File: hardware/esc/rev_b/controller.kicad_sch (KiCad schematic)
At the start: 47 parts, among them J201 ESC_SWD, U201 RP2354B, U204 TPS3430WDRCR, U205 SN74LVC1G08DBVR, U206 TCAN3413DR, U207 MCP2518FD-H/QBB, Y201 12MHz ABM8-272-T3, Y202 40MHz ABM8G

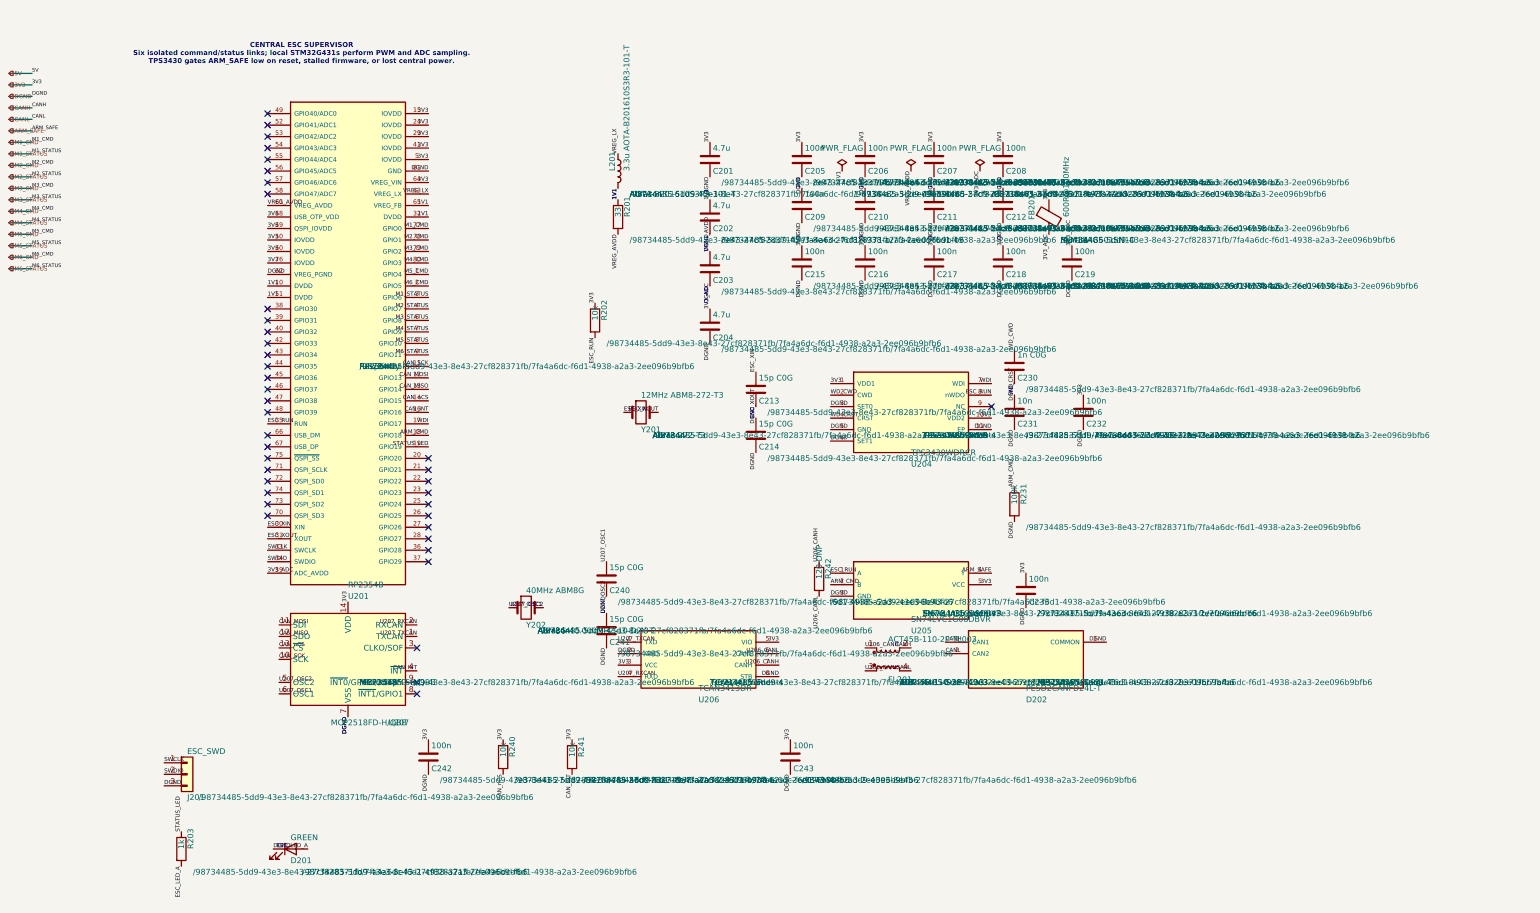
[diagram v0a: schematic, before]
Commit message: fix: consolidate portable Rev-B hardware sources
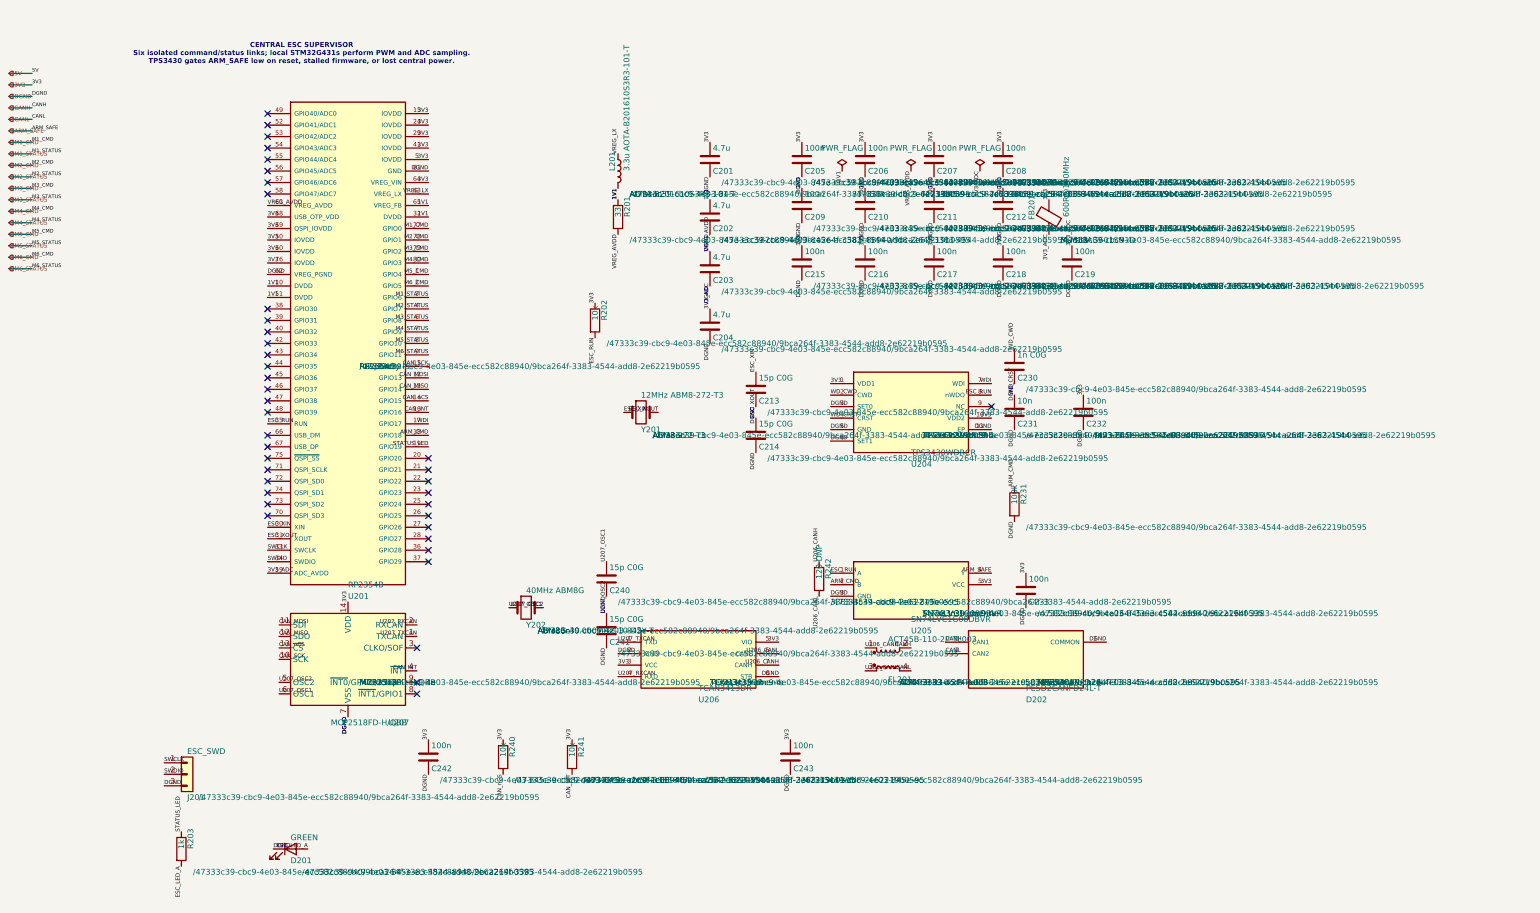
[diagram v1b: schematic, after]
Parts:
- C201, C202, C203, C204, C205, C206, C207, C208, C209, C210, C211, C212, C213, C214, C215, C216, C217, C218, C219, C230, C231, C232, C233, C240, C241, C242, C243, D201, D202, FB201, J201, L201, R201, R202, R203, R231, R240, R241, R242, U201, U204, U205, U206, U207, Y201, Y202: hierarchy_path /98734485-5dd9-43e3-8e43-27cf828371fb/7fa4a6dc-f6d1-4938-a2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 -> /47333c39-cbc9-4e03-845e-ecc582c88940/9bca264f-3383-4544-ad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
- FL201: footprint Inductor_SMD:L_CommonModeChoke_Coilank_ACM4532 -> revb:L_CommonModeChoke_Coilank_ACM4532; hierarchy_path /98734485-5dd9-43e3-8e43-27cf828371fb/7fa4a6dc-f6d1-4938-a2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 -> /47333c39-cbc9-4e03-845e-ecc582c88940/9bca264f-3383-4544-ad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
